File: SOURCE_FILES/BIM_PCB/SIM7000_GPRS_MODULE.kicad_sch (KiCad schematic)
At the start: 49 parts, among them J5 SIM_Card, Q5 BSN20, U2 SIM7000G

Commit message: updates on schematic and complete layout
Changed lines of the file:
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@@
   (symbol (lib_id "Device:LED_Small") (at 276.225 149.225 90) (unit 1)
     (in_bom yes) (on_board yes) (dnp no)
-    (property "Reference" "D13" (at 278.13 149.225 0)
+    (property "Reference" "D13" (at 278.511 149.479 0)
       (effects (font (size 1.27 1.27)))
     )

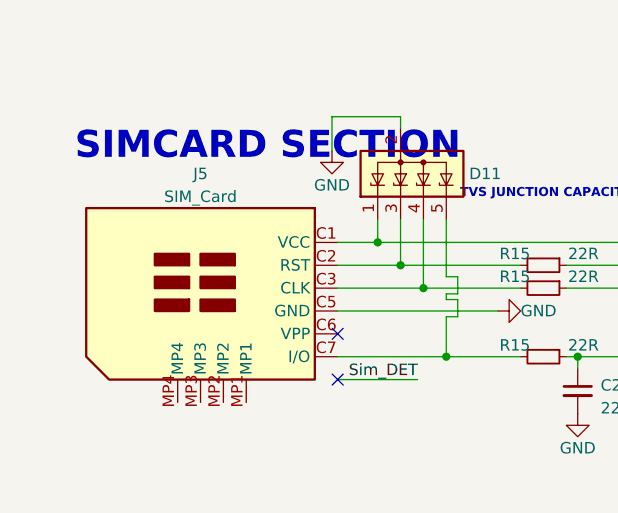
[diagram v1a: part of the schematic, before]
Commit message: completed design PCN and Images
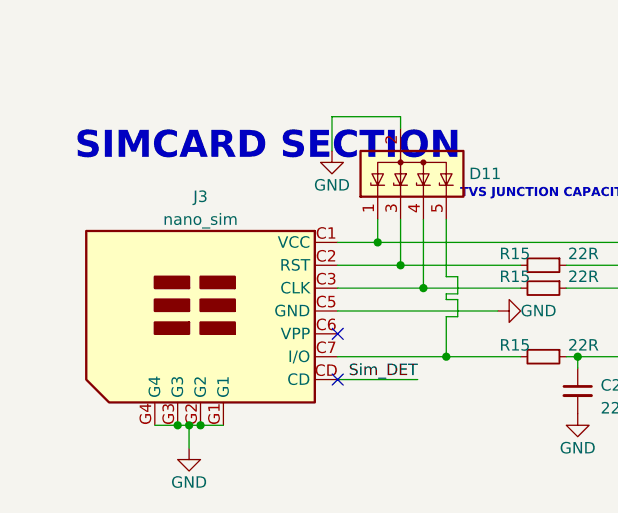
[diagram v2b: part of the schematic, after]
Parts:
- removed J5: SIM_Card, MACHADA_footprints:sim_micro_SMC2026, symbol Connector:SIM_Card
- added J3: nano_sim, greencharge-footprints:GCT_SIM8066-6-1-14-01-A_REVA, symbol MCD_General:nano_sim_SIM8066-6-1-14-01-A
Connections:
- net GND: now also J3.C5 (GND), J3.G1, J3.G2, J3.G3, J3.G4
- net Sim_DET: now also J3.CD
- net V_Sim: now also J3.C1 (VCC)
- net at D11.3 (K), R15.2: now also J3.C2 (RST)
- net at D11.5 (K), R15.2: now also J3.C7 (I/O)
- net at D11.4 (K), R15.2: now also J3.C3 (CLK)
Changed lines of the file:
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@@
   (junction (at 88.9 38.735) (diameter 0) (color 0 0 0 0)
   )
+  (junction (at 26.035 186.69) (diameter 0) (color 0 0 0 0)
+  )
   (junction (at 55.88 179.07) (diameter 0) (color 0 0 0 0)
   )
@@
   (junction (at 186.055 100.965) (diameter 0) (color 0 0 0 0)
   )
+  (junction (at 27.305 186.69) (diameter 0) (color 0 0 0 0)
+  )
   (junction (at 119.38 155.575) (diameter 0) (color 0 0 0 0)
   )
@@
   (junction (at 50.8 24.13) (diameter 0) (color 0 0 0 0)
   )
+  (junction (at 28.575 186.69) (diameter 0) (color 0 0 0 0)
+  )
   (junction (at 43.815 49.53) (diameter 0) (color 0 0 0 0)
   )
@@
     (stroke (width 0) (type default))
   )
+  (wire (pts (xy 28.575 186.69) (xy 31.115 186.69))
+    (stroke (width 0) (type default))
+  )
   (wire (pts (xy 125.095 180.34) (xy 125.095 184.15))
     (stroke (width 0) (type default))
@@
     (stroke (width 0) (type default))
   )
+  (wire (pts (xy 26.035 186.69) (xy 27.305 186.69))
+    (stroke (width 0) (type default))
+  )
   (wire (pts (xy 41.275 49.53) (xy 43.815 49.53))
     (stroke (width 0) (type default))
@@
     (stroke (width 0) (type default))
   )
+  (wire (pts (xy 27.305 186.69) (xy 28.575 186.69))
+    (stroke (width 0) (type default))
+  )
   (wire (pts (xy 73.66 15.24) (xy 61.595 15.24))
     (stroke (width 0) (type default))
@@
     (stroke (width 0) (type default))
   )
+  (wire (pts (xy 23.495 186.69) (xy 26.035 186.69))
+    (stroke (width 0) (type default))
+  )
   (wire (pts (xy 139.7 155.575) (xy 142.24 155.575))
     (stroke (width 0) (type default))
@@
     (stroke (width 0) (type default))
   )
+  (wire (pts (xy 27.305 186.69) (xy 27.305 189.23))
+    (stroke (width 0) (type default))
+  )
   (wire (pts (xy 157.48 74.295) (xy 165.735 74.295))
     (stroke (width 0) (type default))
@@
     )
   )
+  (symbol (lib_id "MCD_General:nano_sim_SIM8066-6-1-14-01-A") (at 31.115 173.99 0) (mirror y) (unit 1)
+    (in_bom yes) (on_board yes) (dnp no) (fields_autoplaced)
+    (property "Reference" "J3" (at 28.575 161.29 0)
+      (effects (font (size 1.27 1.27)))
+    )
+    (property "Value" "nano_sim" (at 28.575 163.83 0)
+      (effects (font (size 1.27 1.27)))
+    )
+    (property "Footprint" "greencharge-footprints:GCT_SIM8066-6-1-14-01-A_REVA" (at 31.115 163.83 0)
+      (effects (font (size 1.27 1.27)) hide)
+    )
+    (property "Datasheet" "https://www.digikey.com/en/products/detail/gct/SIM8066-6-1-14-01-A/14305253?s=N4IgTCBcDaIM4EsC2AOADANgyAugXyA" (at 27.305 161.29 0)
+      (effects (font (size 1.27 1.27)) hide)
+    )
+    (property "MPN" "SIM8066-6-1-14-01-A" (at 31.115 171.45 0)
+      (effects (font (size 1.27 1.27)) hide)
+    )
+    (pin "C1")
+    (pin "C2")
+    (pin "C3")
+    (pin "C5")
+    (pin "C6")
+    (pin "C7")
+    (pin "CD")
+    (pin "G1")
+    (pin "G2")
+    (pin "G3")
+    (pin "G4")
+    (instances
+      (project "GPS_MODULE_V3"
+        (path "/8cb1db64-3fcc-4fb6-aa5a-7b4a50bb28df/341bfb02-419a-4358-97bd-e3e3f41a7556"
+          (reference "J3") (unit 1)
+        )
+      )
+      (project "BIM_PCB"
+        (path "/b79ebed7-e146-448b-8dab-0aefb3e182ca/35710b89-d3a5-410b-ab99-18b25888e68c"
+          (reference "J5") (unit 1)
+        )
+      )
+    )
+  )
   (symbol (lib_id "Filter:B39162B8813P810") (at 223.52 64.135 0) (mirror y) (unit 1)
     (in_bom yes) (on_board yes) (dnp no)
@@
     )
   )
-  (symbol (lib_id "Connector:SIM_Card") (at 31.115 171.45 0) (mirror y) (unit 1)
-    (in_bom yes) (on_board yes) (dnp no) (fields_autoplaced)
-    (property "Reference" "J5" (at 28.575 158.75 0)
-      (effects (font (size 1.27 1.27)))
+  (symbol (lib_id "power:GND") (at 27.305 189.23 0) (unit 1)
+    (in_bom yes) (on_board yes) (dnp no)
+    (property "Reference" "#PWR032" (at 27.305 195.58 0)
+      (effects (font (size 1.27 1.27)) hide)
     )
-    (property "Value" "SIM_Card" (at 28.575 161.29 0)
+    (property "Value" "GND" (at 27.305 193.04 0)
       (effects (font (size 1.27 1.27)))
     )
-    (property "Footprint" "MACHADA_footprints:sim_micro_SMC2026" (at 31.115 161.29 0)
+    (property "Footprint" "" (at 27.305 189.23 0)
       (effects (font (size 1.27 1.27)) hide)
     )
-    (property "Datasheet" " ~" (at 27.305 158.75 0)
+    (property "Datasheet" "" (at 27.305 189.23 0)
       (effects (font (size 1.27 1.27)) hide)
     )
-    (pin "C1")
-    (pin "C2")
-    (pin "C3")
-    (pin "C4")
-    (pin "C5")
-    (pin "C6")
-    (pin "C7")
-    (pin "C8")
-    (pin "MP1")
-    (pin "MP2")
-    (pin "MP3")
-    (pin "MP4")
+    (pin "1")
     (instances
+      (project "SIM7000G_GPS_GPRS_MODULE"
+        (path "/682fa917-2f52-4469-aa75-8536293ede48"
+          (reference "#PWR032") (unit 1)
+        )
+      )
+      (project "GPS_MODULE_V3"
+        (path "/8cb1db64-3fcc-4fb6-aa5a-7b4a50bb28df/341bfb02-419a-4358-97bd-e3e3f41a7556"
+          (reference "#PWR021") (unit 1)
+        )
+      )
+      (project "proxy_obdII_logger_hardware"
+        (path "/a2f77e01-8fcf-4cc1-94c1-b0f4d49b6e4a/29e00ce2-594a-4b20-a91d-a5731986a14b"
+          (reference "#PWR032") (unit 1)
+        )
+      )
+      (project "Weather_Station_Project"
+        (path "/aaf5c359-cd8c-4cad-b3ec-83c1a2a58ae1/ca140549-f0a4-476c-ad7f-ae707a64a42e"
+          (reference "#PWR053") (unit 1)
+        )
+      )
       (project "BIM_PCB"
         (path "/b79ebed7-e146-448b-8dab-0aefb3e182ca/35710b89-d3a5-410b-ab99-18b25888e68c"
-          (reference "J5") (unit 1)
+          (reference "#PWR0120") (unit 1)
+        )
+      )
+      (project "SIM_Module_Interface"
+        (path "/d4bab6f2-6f98-4591-bf22-3c5c715b9155"
+          (reference "#PWR032") (unit 1)
+        )
+      )
+      (project "ELIESTER_V2"
+        (path "/efe55700-0211-4481-aa01-7a7eb74def17/414f1577-4ce3-43d7-bbf4-7827eef840c4"
+          (reference "#PWR0132") (unit 1)
         )
       )

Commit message: complete BIM Board
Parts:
- C20: value 100u -> 1000u; footprint Capacitor_Tantalum_SMD:CP_EIA-3216-18_Kemet-A -> Capacitor_Tantalum_SMD:CP_EIA-7343-43_Kemet-X; MPN TLJA107M006R0800 -> T491X108K006AT
- J3: footprint greencharge-footprints:GCT_SIM8066-6-1-14-01-A_REVA -> MACHADA_footprints:nano_sim_NSIM-2-C; MPN SIM8066-6-1-14-01-A -> NSIM-2-C
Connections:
- net GND: now also J3.MP1; no longer J3.G1, J3.G2, J3.G3, J3.G4
- net Sim_DET: no longer J3.CD
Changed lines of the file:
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@@
   (junction (at 88.9 38.735) (diameter 0) (color 0 0 0 0)
   )
-  (junction (at 26.035 186.69) (diameter 0) (color 0 0 0 0)
-  )
   (junction (at 55.88 179.07) (diameter 0) (color 0 0 0 0)
   )
@@
   (junction (at 186.055 100.965) (diameter 0) (color 0 0 0 0)
   )
-  (junction (at 27.305 186.69) (diameter 0) (color 0 0 0 0)
-  )
   (junction (at 119.38 155.575) (diameter 0) (color 0 0 0 0)
   )
@@
   (junction (at 50.8 24.13) (diameter 0) (color 0 0 0 0)
   )
-  (junction (at 28.575 186.69) (diameter 0) (color 0 0 0 0)
-  )
   (junction (at 43.815 49.53) (diameter 0) (color 0 0 0 0)
   )
@@
   (no_connect (at 157.48 120.015))
   (no_connect (at 96.52 103.505))
+  (no_connect (at 43.815 181.61))
   (no_connect (at 96.52 122.555))
   (no_connect (at 157.48 122.555))
   (no_connect (at 96.52 108.585))
-  (no_connect (at 43.815 181.61))
   (no_connect (at 43.815 176.53))
   (no_connect (at 96.52 111.125))
@@
     (stroke (width 0) (type default))
   )
-  (wire (pts (xy 28.575 186.69) (xy 31.115 186.69))
-    (stroke (width 0) (type default))
-  )
   (wire (pts (xy 125.095 180.34) (xy 125.095 184.15))
     (stroke (width 0) (type default))
@@
     (stroke (width 0) (type default))
   )
-  (wire (pts (xy 26.035 186.69) (xy 27.305 186.69))
-    (stroke (width 0) (type default))
-  )
   (wire (pts (xy 41.275 49.53) (xy 43.815 49.53))
     (stroke (width 0) (type default))
@@
     (stroke (width 0) (type default))
   )
-  (wire (pts (xy 27.305 186.69) (xy 28.575 186.69))
-    (stroke (width 0) (type default))
-  )
   (wire (pts (xy 73.66 15.24) (xy 61.595 15.24))
     (stroke (width 0) (type default))
@@
     (stroke (width 0) (type default))
   )
-  (wire (pts (xy 23.495 186.69) (xy 26.035 186.69))
-    (stroke (width 0) (type default))
-  )
   (wire (pts (xy 139.7 155.575) (xy 142.24 155.575))
     (stroke (width 0) (type default))
@@
     (stroke (width 0) (type default))
   )
-  (wire (pts (xy 27.305 186.69) (xy 27.305 189.23))
+  (wire (pts (xy 31.115 186.69) (xy 31.115 189.23))
     (stroke (width 0) (type default))
   )
@@
       (effects (font (size 1.27 1.27)))
     )
-    (property "Footprint" "greencharge-footprints:GCT_SIM8066-6-1-14-01-A_REVA" (at 31.115 163.83 0)
+    (property "Footprint" "MACHADA_footprints:nano_sim_NSIM-2-C" (at 31.115 163.83 0)
       (effects (font (size 1.27 1.27)) hide)
     )
@@
       (effects (font (size 1.27 1.27)) hide)
     )
-    (property "MPN" "SIM8066-6-1-14-01-A" (at 31.115 171.45 0)
+    (property "MPN" "NSIM-2-C" (at 31.115 171.45 0)
       (effects (font (size 1.27 1.27)) hide)
     )
@@
     (pin "C6")
     (pin "C7")
-    (pin "CD")
-    (pin "G1")
-    (pin "G2")
-    (pin "G3")
-    (pin "G4")
+    (pin "MP1")
     (instances
       (project "GPS_MODULE_V3"
@@
   (symbol (lib_id "Device:C_Polarized") (at 101.6 33.02 0) (unit 1)
     (in_bom yes) (on_board yes) (dnp no) (fields_autoplaced)
-    (property "Reference" "C20" (at 104.775 31.496 0)
+    (property "Reference" "C20" (at 105.41 31.496 0)
       (effects (font (size 1.27 1.27)) (justify left))
     )
-    (property "Value" "100u" (at 104.775 34.036 0)
+    (property "Value" "1000u" (at 105.41 34.036 0)
       (effects (font (size 1.27 1.27)) (justify left))
     )
-    (property "Footprint" "Capacitor_Tantalum_SMD:CP_EIA-3216-18_Kemet-A" (at 102.5652 36.83 0)
+    (property "Footprint" "Capacitor_Tantalum_SMD:CP_EIA-7343-43_Kemet-X" (at 102.5652 36.83 0)
       (effects (font (size 1.27 1.27)) hide)
     )
@@
       (effects (font (size 1.27 1.27)) hide)
     )
-    (property "MPN" "TLJA107M006R0800" (at 101.6 33.02 0)
+    (property "MPN" "T491X108K006AT" (at 101.6 33.02 0)
       (effects (font (size 1.27 1.27)) hide)
     )
@@
     )
   )
-  (symbol (lib_id "power:GND") (at 27.305 189.23 0) (unit 1)
+  (symbol (lib_id "power:GND") (at 31.115 189.23 0) (unit 1)
     (in_bom yes) (on_board yes) (dnp no)
-    (property "Reference" "#PWR032" (at 27.305 195.58 0)
+    (property "Reference" "#PWR032" (at 31.115 195.58 0)
       (effects (font (size 1.27 1.27)) hide)
     )
-    (property "Value" "GND" (at 27.305 193.04 0)
+    (property "Value" "GND" (at 31.115 193.04 0)
       (effects (font (size 1.27 1.27)))
     )
-    (property "Footprint" "" (at 27.305 189.23 0)
+    (property "Footprint" "" (at 31.115 189.23 0)
       (effects (font (size 1.27 1.27)) hide)
     )
-    (property "Datasheet" "" (at 27.305 189.23 0)
+    (property "Datasheet" "" (at 31.115 189.23 0)
       (effects (font (size 1.27 1.27)) hide)
     )

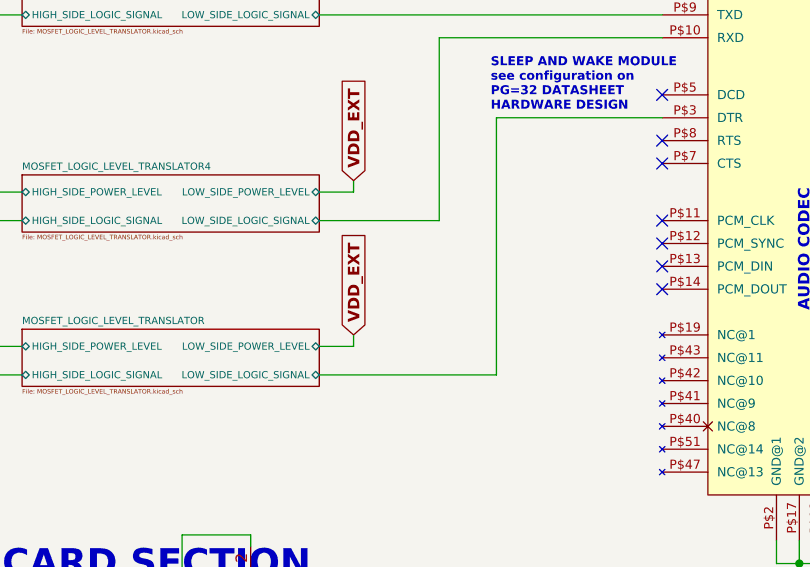
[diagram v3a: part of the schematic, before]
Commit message: update to A9G and connector
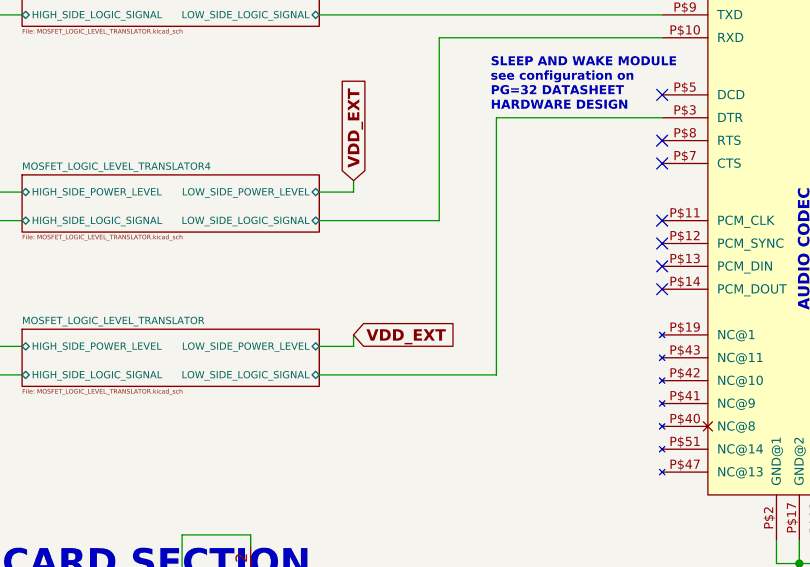
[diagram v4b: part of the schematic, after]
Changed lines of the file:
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@@
     )
   )
-  (global_label "VDD_EXT" (shape input) (at 62.23 130.175 90) (fields_autoplaced)
+  (global_label "VDD_EXT" (shape input) (at 62.23 130.175 0) (fields_autoplaced)
     (effects (font (size 1.27 1.27) bold) (justify left))
-    (property "Intersheetrefs" "${INTERSHEET_REFS}" (at 62.23 118.9185 90)
+    (property "Intersheetrefs" "${INTERSHEET_REFS}" (at 73.4865 130.175 0)
       (effects (font (size 1.27 1.27)) (justify left) hide)
     )
